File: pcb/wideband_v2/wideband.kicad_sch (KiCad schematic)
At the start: 45 parts, among them Q1 BTS3028, U10 XC6206P332MR, U7 MCP6004, U8 AD8628, U9 REF3033

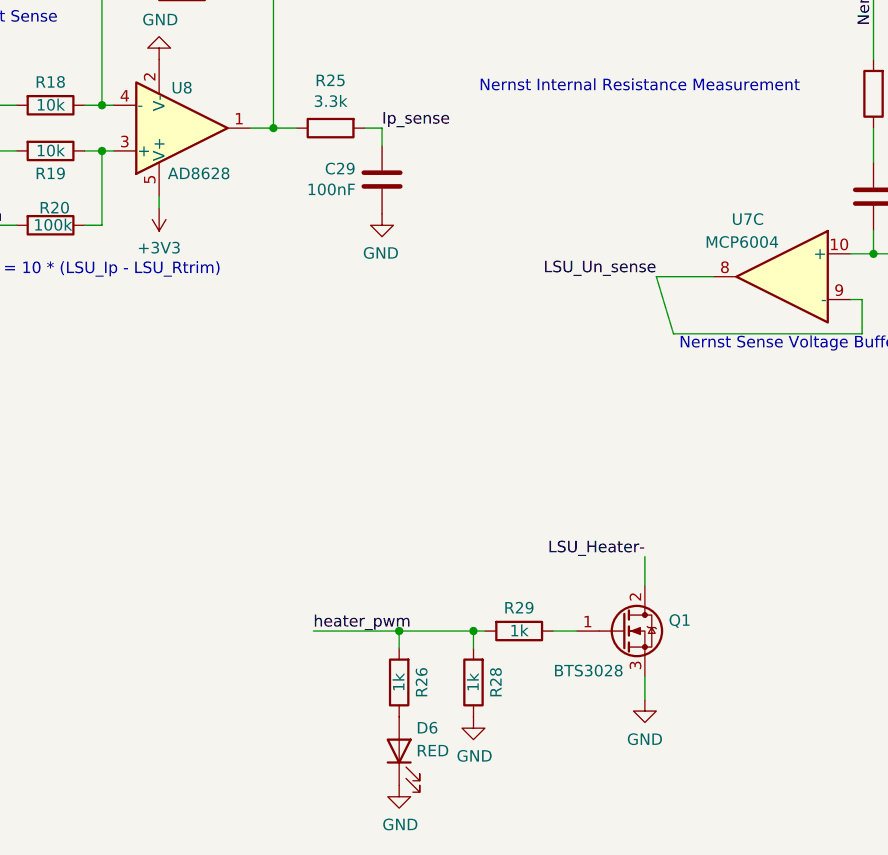
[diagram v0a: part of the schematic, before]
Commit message: BTS3028 => WSF60N06 | AD8628 => OPA388IDR
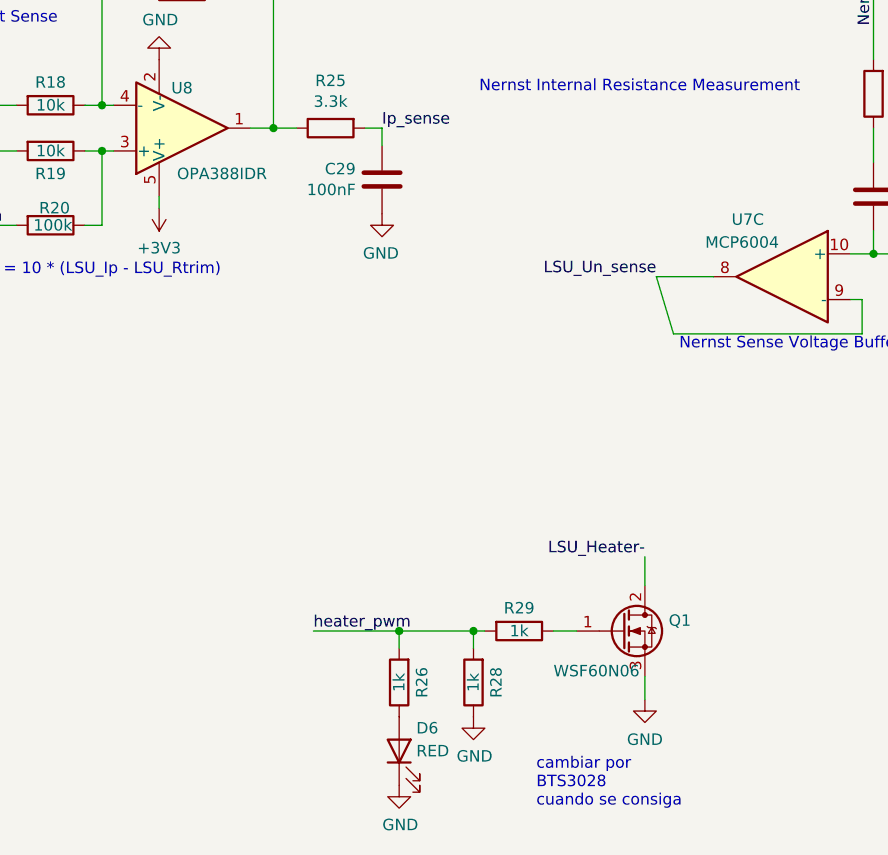
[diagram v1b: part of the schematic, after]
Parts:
- Q1: value BTS3028 -> WSF60N06; LCSC C112639 -> C148432
- U8: value AD8628 -> OPA388IDR; LCSC C29309 -> C154118
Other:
- note added: "cambiar por BTS3028 cuando se consiga"
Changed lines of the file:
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@@
+    (effects (font (size 1.27 1.27)) (justify left bottom))
+  )
+  (text "cambiar por\nBTS3028\ncuando se consiga" (at 139.7 189.865 0)
     (effects (font (size 1.27 1.27)) (justify left bottom))
   )
@@
     (in_bom yes) (on_board yes)
     (property "Reference" "U8" (id 0) (at 100.33 109.855 0))
-    (property "Value" "AD8628" (id 1) (at 102.235 119.38 0))
+    (property "Value" "OPA388IDR" (id 1) (at 104.775 119.38 0))
     (property "Footprint" "Package_TO_SOT_SMD:TSOT-23-5" (id 2) (at 100.33 114.3 0)
       (effects (font (size 1.27 1.27)) hide)
@@
       (effects (font (size 1.27 1.27)) hide)
     )
-    (property "LCSC" "C29309" (id 4) (at 100.33 114.3 0)
+    (property "LCSC" "C154118" (id 4) (at 100.33 114.3 0)
       (effects (font (size 1.27 1.27)) hide)
     )
@@
       (effects (font (size 1.27 1.27)) (justify left))
     )
-    (property "Value" "BTS3028" (id 1) (at 141.605 174.625 0)
+    (property "Value" "WSF60N06" (id 1) (at 141.605 174.625 0)
       (effects (font (size 1.27 1.27)) (justify left))
     )
@@
       (effects (font (size 1.27 1.27)) hide)
     )
-    (property "LCSC" "C112639" (id 4) (at 149.225 170.18 0)
-      (effects (font (size 1.27 1.27)) hide)
-    )
+    (property "LCSC" "C148432" (id 4) (at 149.225 170.18 0)
+      (effects (font (size 1.27 1.27)) hide)
+    )
